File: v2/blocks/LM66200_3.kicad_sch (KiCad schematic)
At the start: 2 parts, among them U7 C3235556 (M66200DRLR)

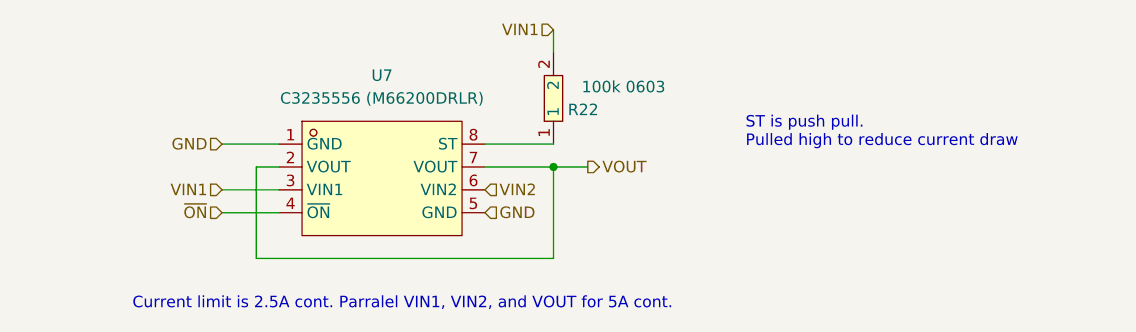
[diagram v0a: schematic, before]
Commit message: preliminary layout
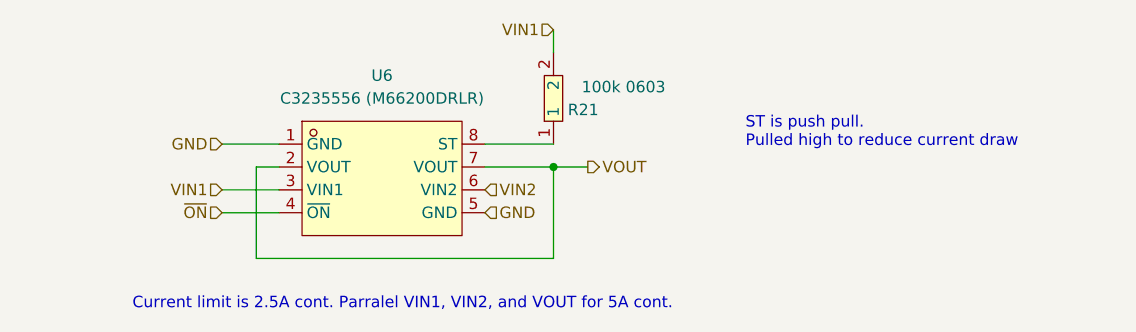
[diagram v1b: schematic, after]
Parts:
- renumbered R22 to R21, U7 to U6
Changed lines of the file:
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@@
 		(dnp no)
 		(fields_autoplaced yes)
-		(property "Reference" "U7"
+		(property "Reference" "U6"
 			(at 101.6 44.45 0)
 			(effects
@@
 			(project "EPSv1"
 				(path "/61d36b12-c329-4dd2-b08b-b63678fc7b25/4efb8ab3-6299-4c47-a3d6-e147e289017f"
-					(reference "U7")
+					(reference "U6")
 					(unit 1)
 				)
@@
 		(on_board yes)
 		(dnp no)
-		(property "Reference" "R22"
+		(property "Reference" "R21"
 			(at 123.952 48.26 90)
 			(effects
@@
 			(project "EPSv1"
 				(path "/61d36b12-c329-4dd2-b08b-b63678fc7b25/4efb8ab3-6299-4c47-a3d6-e147e289017f"
-					(reference "R22")
+					(reference "R21")
 					(unit 1)
 				)

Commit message: routing done
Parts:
- renumbered R21 to R25, U6 to U7
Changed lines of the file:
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@@
 		(dnp no)
 		(fields_autoplaced yes)
-		(property "Reference" "U6"
+		(property "Reference" "U7"
 			(at 101.6 44.45 0)
 			(effects
@@
 			(project "EPSv1"
 				(path "/61d36b12-c329-4dd2-b08b-b63678fc7b25/4efb8ab3-6299-4c47-a3d6-e147e289017f"
-					(reference "U6")
+					(reference "U7")
 					(unit 1)
 				)
@@
 		(on_board yes)
 		(dnp no)
-		(property "Reference" "R21"
+		(property "Reference" "R25"
 			(at 123.952 48.26 90)
 			(effects
@@
 			(project "EPSv1"
 				(path "/61d36b12-c329-4dd2-b08b-b63678fc7b25/4efb8ab3-6299-4c47-a3d6-e147e289017f"
-					(reference "R21")
+					(reference "R25")
 					(unit 1)
 				)

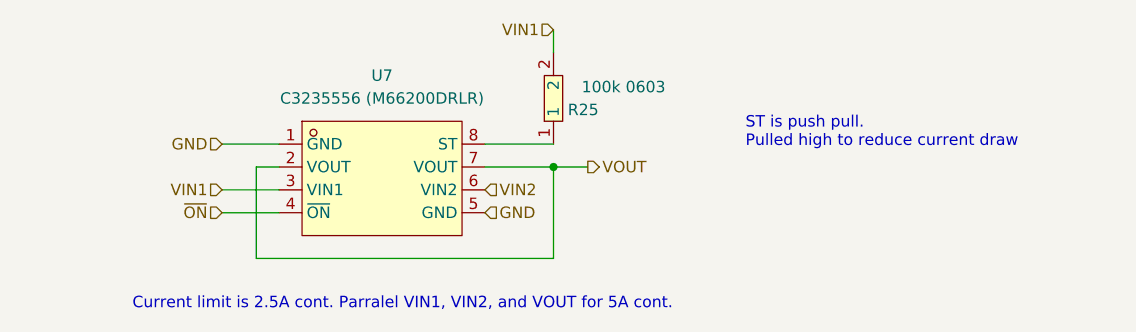
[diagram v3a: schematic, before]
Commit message: can transceiver and battery reverse polarity bypass
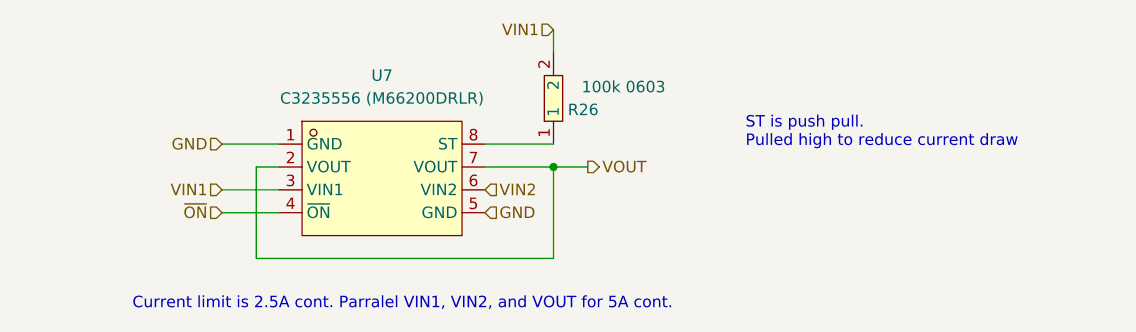
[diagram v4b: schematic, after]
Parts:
- renumbered R25 to R26
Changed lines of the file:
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@@
 		(shape output)
 		(at 124.46 54.61 0)
+		(fields_autoplaced yes)
 		(effects
 			(font
@@
 		(shape input)
 		(at 83.82 52.07 180)
+		(fields_autoplaced yes)
 		(effects
 			(font
@@
 		(shape input)
 		(at 113.03 59.69 0)
+		(fields_autoplaced yes)
 		(effects
 			(font
@@
 		(shape input)
 		(at 83.82 59.69 180)
+		(fields_autoplaced yes)
 		(effects
 			(font
@@
 		(shape input)
 		(at 120.65 39.37 180)
+		(fields_autoplaced yes)
 		(effects
 			(font
@@
 		(shape input)
 		(at 113.03 57.15 0)
+		(fields_autoplaced yes)
 		(effects
 			(font
@@
 		(shape input)
 		(at 83.82 57.15 180)
+		(fields_autoplaced yes)
 		(effects
 			(font
@@
 		(on_board yes)
 		(dnp no)
-		(property "Reference" "R25"
+		(property "Reference" "R26"
 			(at 123.952 48.26 90)
 			(effects
@@
 			(project "EPSv1"
 				(path "/61d36b12-c329-4dd2-b08b-b63678fc7b25/4efb8ab3-6299-4c47-a3d6-e147e289017f"
-					(reference "R25")
+					(reference "R26")
 					(unit 1)
 				)
